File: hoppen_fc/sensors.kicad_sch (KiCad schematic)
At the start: 12 parts, among them U2 MMC5983MA, U3 BMI088, U4 MS5607-02BA

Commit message: finished adding lcsc numbers
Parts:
- added S1: ~, 0_misc:right_hand_rule, symbol 0_misc:right_hand_rule
- C53: renamed from C28; LCSC (none) -> C19666
- C54: renamed from C30; LCSC (none) -> C307331
- C55: renamed from C31; LCSC (none) -> C307331
- C56: renamed from C34; LCSC (none) -> C19666
- C57: renamed from C35; LCSC (none) -> C307331
- C58: renamed from C27; LCSC (none) -> C19666
- C59: renamed from C29; LCSC (none) -> C307331
- C60: renamed from C32; LCSC (none) -> C307331
- C61: renamed from C33; LCSC (none) -> C307331
- renumbered U4 to U7, U3 to U8, U2 to U9

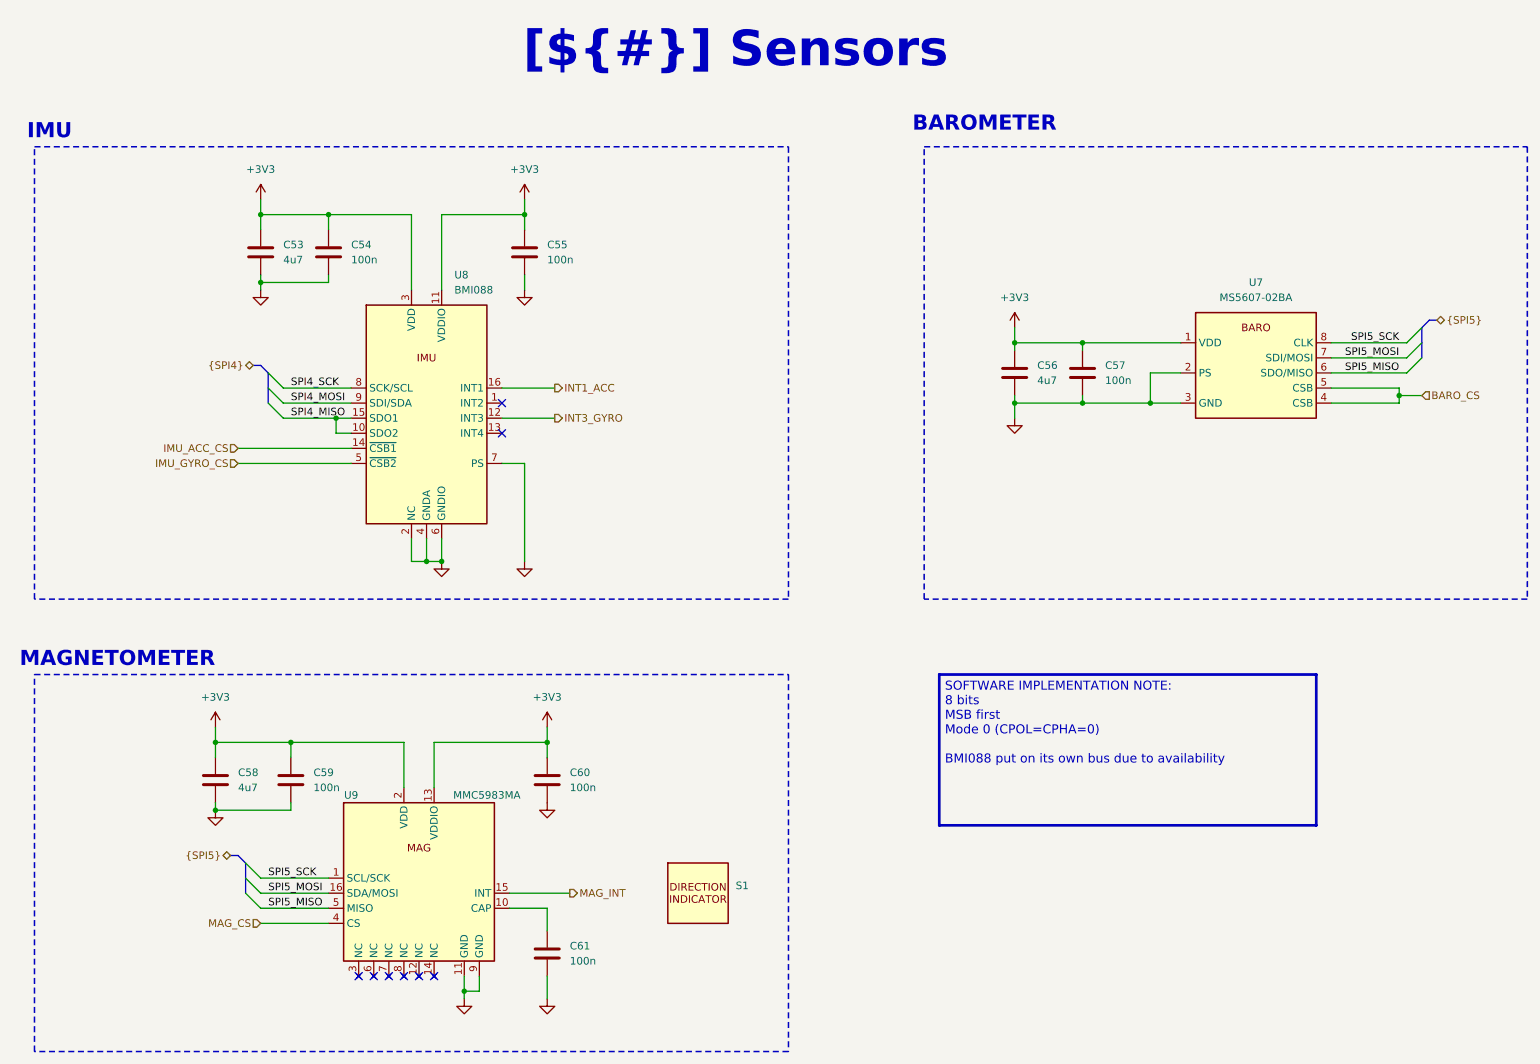
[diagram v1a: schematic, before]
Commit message: routing and adding rf module
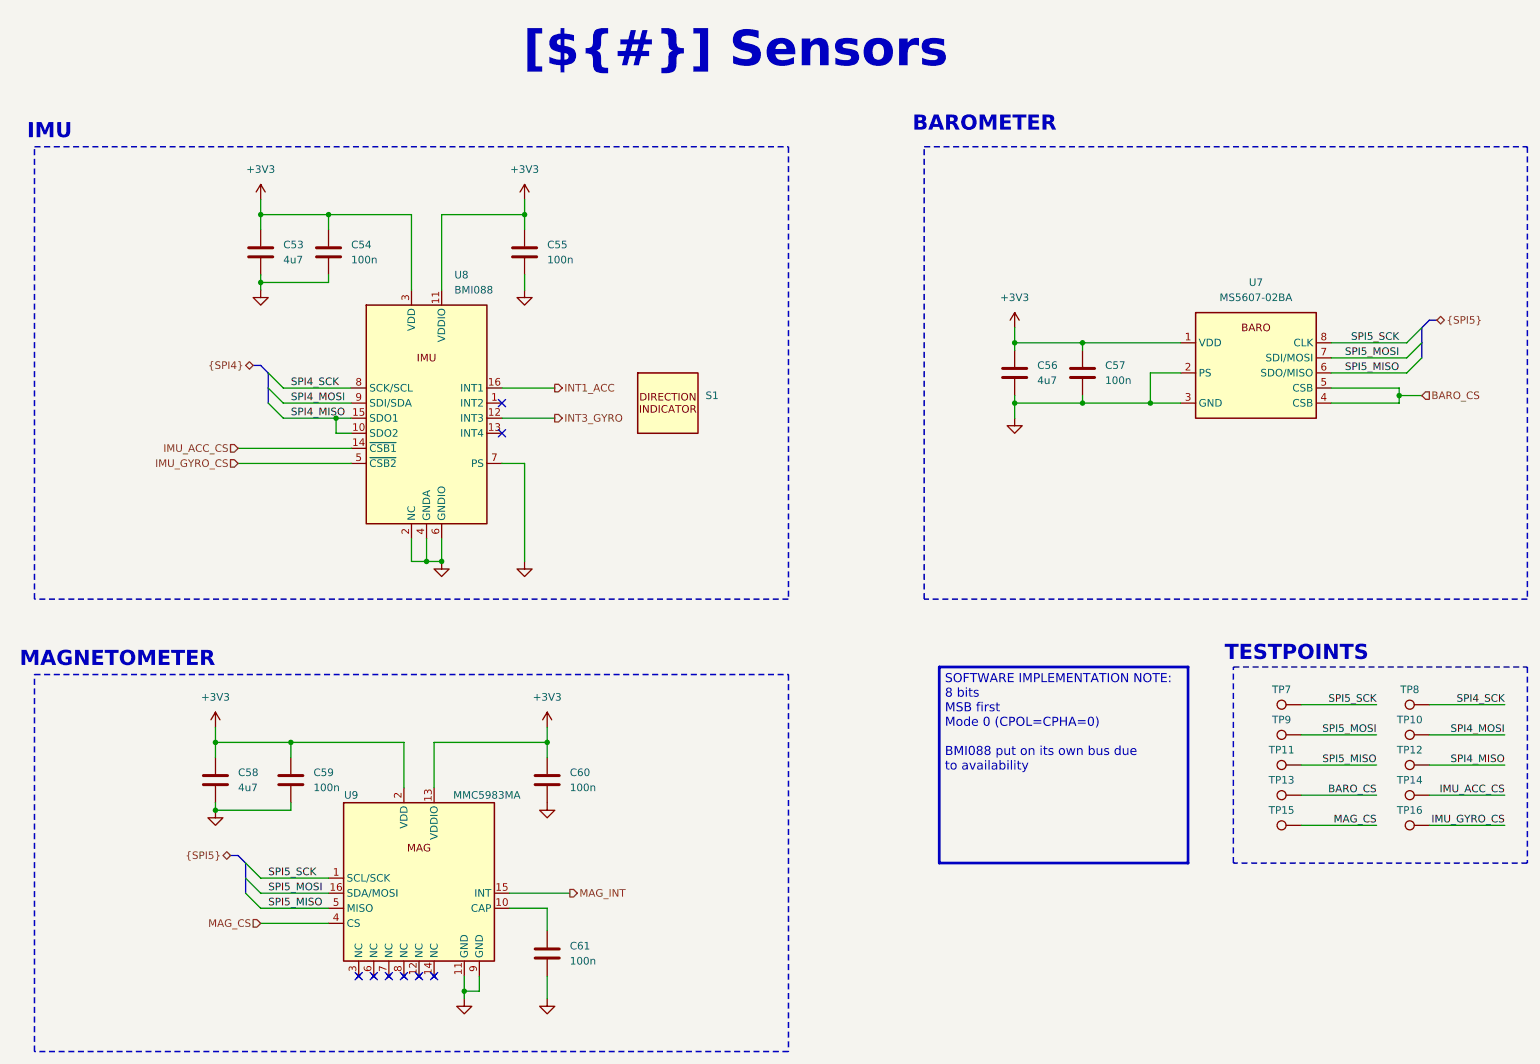
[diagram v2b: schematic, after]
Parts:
- added TP10, TP11, TP12, TP13, TP14, TP15, TP16, TP7, TP8, TP9: TestPoint, TestPoint:TestPoint_Pad_1.0x1.0mm, symbol Connector:TestPoint
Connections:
- net BARO_CS: now also TP13.1
- net IMU_ACC_CS: now also TP14.1
- net IMU_GYRO_CS: now also TP16.1
- net MAG_CS: now also TP15.1
- net SPI4_MISO: now also TP12.1
- net SPI4_MOSI: now also TP10.1
- net SPI4_SCK: now also TP8.1
- net SPI5_MISO: now also TP11.1
- net SPI5_MOSI: now also TP9.1
- net SPI5_SCK: now also TP7.1
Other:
- note added: "TESTPOINTS"
- moved on the sheet: S1

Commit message: bump
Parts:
- renumbered TP11 to TP10, TP12 to TP11, TP13 to TP12, TP14 to TP13, TP15 to TP14, TP16 to TP15, TP7 to TP6, TP8 to TP7, TP9 to TP8, TP10 to TP9
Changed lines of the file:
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@@
 		(dnp no)
 		(fields_autoplaced yes)
-		(property "Reference" "TP14"
+		(property "Reference" "TP13"
 			(at 257.048 144.78 90)
 			(effects
@@
 			(project "hoppen_fc"
 				(path "/abe950a1-9eef-4508-9fd4-31d3e723e029/c85454e5-a89e-41eb-a5ed-71b4fc4cf13a/328607b5-eaf8-4cbb-82fe-138ea1b53a88"
-					(reference "TP14")
+					(reference "TP13")
 					(unit 1)
 				)
@@
 		(dnp no)
 		(fields_autoplaced yes)
-		(property "Reference" "TP11"
+		(property "Reference" "TP10"
 			(at 235.458 139.7 90)
 			(effects
@@
 			(project "hoppen_fc"
 				(path "/abe950a1-9eef-4508-9fd4-31d3e723e029/c85454e5-a89e-41eb-a5ed-71b4fc4cf13a/328607b5-eaf8-4cbb-82fe-138ea1b53a88"
-					(reference "TP11")
+					(reference "TP10")
 					(unit 1)
 				)
@@
 		(dnp no)
 		(fields_autoplaced yes)
-		(property "Reference" "TP16"
+		(property "Reference" "TP15"
 			(at 257.048 149.86 90)
 			(effects
@@
 			(project "hoppen_fc"
 				(path "/abe950a1-9eef-4508-9fd4-31d3e723e029/c85454e5-a89e-41eb-a5ed-71b4fc4cf13a/328607b5-eaf8-4cbb-82fe-138ea1b53a88"
-					(reference "TP16")
+					(reference "TP15")
 					(unit 1)
 				)
@@
 		(dnp no)
 		(fields_autoplaced yes)
-		(property "Reference" "TP13"
+		(property "Reference" "TP12"
 			(at 235.458 144.78 90)
 			(effects
@@
 			(project "hoppen_fc"
 				(path "/abe950a1-9eef-4508-9fd4-31d3e723e029/c85454e5-a89e-41eb-a5ed-71b4fc4cf13a/328607b5-eaf8-4cbb-82fe-138ea1b53a88"
-					(reference "TP13")
+					(reference "TP12")
 					(unit 1)
 				)
@@
 		(dnp no)
 		(fields_autoplaced yes)
-		(property "Reference" "TP7"
+		(property "Reference" "TP6"
 			(at 235.458 129.54 90)
 			(effects
@@
 			(project "hoppen_fc"
 				(path "/abe950a1-9eef-4508-9fd4-31d3e723e029/c85454e5-a89e-41eb-a5ed-71b4fc4cf13a/328607b5-eaf8-4cbb-82fe-138ea1b53a88"
-					(reference "TP7")
+					(reference "TP6")
 					(unit 1)
 				)
@@
 		(dnp no)
 		(fields_autoplaced yes)
-		(property "Reference" "TP15"
+		(property "Reference" "TP14"
 			(at 235.458 149.86 90)
 			(effects
@@
 			(project "hoppen_fc"
 				(path "/abe950a1-9eef-4508-9fd4-31d3e723e029/c85454e5-a89e-41eb-a5ed-71b4fc4cf13a/328607b5-eaf8-4cbb-82fe-138ea1b53a88"
-					(reference "TP15")
+					(reference "TP14")
 					(unit 1)
 				)
@@
 		(dnp no)
 		(fields_autoplaced yes)
-		(property "Reference" "TP10"
+		(property "Reference" "TP9"
 			(at 257.048 134.62 90)
 			(effects
@@
 			(project "hoppen_fc"
 				(path "/abe950a1-9eef-4508-9fd4-31d3e723e029/c85454e5-a89e-41eb-a5ed-71b4fc4cf13a/328607b5-eaf8-4cbb-82fe-138ea1b53a88"
-					(reference "TP10")
+					(reference "TP9")
 					(unit 1)
 				)
@@
 		(dnp no)
 		(fields_autoplaced yes)
-		(property "Reference" "TP12"
+		(property "Reference" "TP11"
 			(at 257.048 139.7 90)
 			(effects
@@
 			(project "hoppen_fc"
 				(path "/abe950a1-9eef-4508-9fd4-31d3e723e029/c85454e5-a89e-41eb-a5ed-71b4fc4cf13a/328607b5-eaf8-4cbb-82fe-138ea1b53a88"
-					(reference "TP12")
+					(reference "TP11")
 					(unit 1)
 				)
@@
 		(dnp no)
 		(fields_autoplaced yes)
-		(property "Reference" "TP9"
+		(property "Reference" "TP8"
 			(at 235.458 134.62 90)
 			(effects
@@
 			(project "hoppen_fc"
 				(path "/abe950a1-9eef-4508-9fd4-31d3e723e029/c85454e5-a89e-41eb-a5ed-71b4fc4cf13a/328607b5-eaf8-4cbb-82fe-138ea1b53a88"
-					(reference "TP9")
+					(reference "TP8")
 					(unit 1)
 				)
@@
 		(dnp no)
 		(fields_autoplaced yes)
-		(property "Reference" "TP8"
+		(property "Reference" "TP7"
 			(at 257.048 129.54 90)
 			(effects
@@
 			(project "hoppen_fc"
 				(path "/abe950a1-9eef-4508-9fd4-31d3e723e029/c85454e5-a89e-41eb-a5ed-71b4fc4cf13a/328607b5-eaf8-4cbb-82fe-138ea1b53a88"
-					(reference "TP8")
-					(unit 1)
-				)
+					(reference "TP7")
+					(unit 1)
+				)

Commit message: bump
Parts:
- removed C53, C56: 4u7, 0_capacitor_smd:C_0603_1608Metric, symbol Device:C
- removed C54, C55, C57, C59, C61: 100n, 0_capacitor_smd:C_0402_1005Metric, symbol Device:C
- added C46, C47, C48: 100n, 0_capacitor_smd:C_0402_1005Metric, symbol Device:C
- added C51: 10u, 0_capacitor_smd:C_0805_2012Metric, symbol Device:C
- added TP17, TP18, TP19: TestPoint, TestPoint:TestPoint_Pad_1.0x1.0mm, symbol Connector:TestPoint
- C49: renamed from C58; value 4u7 -> 1u; footprint 0_capacitor_smd:C_0603_1608Metric -> 0_capacitor_smd:C_0402_1005Metric; LCSC C19666 -> C52923
- renumbered C60 to C50, TP9 to TP10, TP10 to TP11, TP11 to TP12, TP12 to TP13, TP13 to TP14, TP14 to TP15, TP15 to TP16, TP6 to TP7, TP7 to TP8, TP8 to TP9, U9 to U10, U7 to U8, U8 to U9
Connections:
- net +3V3: now also C46.1, C47.1, C48.1
- net GND: now also C46.2, C47.2, C48.2, C51.1
- net INT1_ACC: now also TP18.1
- net INT3_GYRO: now also TP19.1
- net MAG_INT: now also TP17.1
- net SPI4_MISO: now also U10.5 (MISO), U8.6 (SDO/MISO); no longer U9.10 (SDO2), U9.15 (SDO1)
- net SPI4_MOSI: now also U10.16 (SDA/MOSI), U8.7 (SDI/MOSI); no longer U9.9 (SDI/SDA)
- net SPI4_SCK: now also U10.1 (SCL/SCK), U8.8 (CLK); no longer U9.8 (SCK/SCL)
- net MAG_CAP: now reaches U10.10 (CAP)
- net MAG_CAP: now also C51.2
- removed net SPI5_MISO: TP11.1, U10.5 (MISO), U8.6 (SDO/MISO)
- removed net SPI5_MOSI: TP9.1, U10.16 (SDA/MOSI), U8.7 (SDI/MOSI)
- removed net SPI5_SCK: TP7.1, U10.1 (SCL/SCK), U8.8 (CLK)
- new net SPI1_MISO: TP11.1, U9.10 (SDO2), U9.15 (SDO1)
- new net SPI1_MOSI: TP9.1, U9.9 (SDI/SDA)
- new net SPI1_SCK: TP7.1, U9.8 (SCK/SCL)
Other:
- moved on the sheet: C49, TP10, TP11, TP12, TP13, TP14, TP15, TP16, TP7, TP8, TP9

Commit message: bump
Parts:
- added S2: ~, 0_misc:right_hand_rule_2, symbol 0_misc:right_hand_rule
- renumbered TP7 to TP23, TP8 to TP24, TP9 to TP25, TP10 to TP26, TP11 to TP27, TP12 to TP28, TP13 to TP29, TP14 to TP30, TP15 to TP31, TP16 to TP32, TP17 to TP33, TP18 to TP34, TP19 to TP35
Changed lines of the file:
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@@
+	)
+	(symbol
+		(lib_id "0_misc:right_hand_rule")
+		(at 134.62 165.1 0)
+		(unit 1)
+		(exclude_from_sim no)
+		(in_bom no)
+		(on_board yes)
+		(dnp no)
+		(fields_autoplaced yes)
+		(property "Reference" "S2"
+			(at 140.97 163.8299 0)
+			(effects
+				(font
+					(size 1.27 1.27)
+				)
+				(justify left)
+			)
+		)
+		(property "Value" "~"
+			(at 140.97 166.3699 0)
+			(effects
+				(font
+					(size 1.27 1.27)
+				)
+				(justify left)
+				(hide yes)
+			)
+		)
+		(property "Footprint" "0_misc:right_hand_rule_2"
+			(at 134.62 165.1 0)
+			(effects
+				(font
+					(size 1.27 1.27)
+				)
+				(hide yes)
+			)
+		)
+		(property "Datasheet" ""
+			(at 134.62 165.1 0)
+			(effects
+				(font
+					(size 1.27 1.27)
+				)
+				(hide yes)
+			)
+		)
+		(property "Description" ""
+			(at 134.62 165.1 0)
+			(effects
+				(font
+					(size 1.27 1.27)
+				)
+				(hide yes)
+			)
+		)
+		(instances
+			(project "hoppen_fc"
+				(path "/abe950a1-9eef-4508-9fd4-31d3e723e029/c85454e5-a89e-41eb-a5ed-71b4fc4cf13a/328607b5-eaf8-4cbb-82fe-138ea1b53a88"
+					(reference "S2")
+					(unit 1)
+				)
+			)
+		)
 	)
 	(symbol
@@
 		(dnp no)
 		(fields_autoplaced yes)
-		(property "Reference" "TP14"
+		(property "Reference" "TP30"
 			(at 257.048 142.24 90)
 			(effects
@@
 			(project "hoppen_fc"
 				(path "/abe950a1-9eef-4508-9fd4-31d3e723e029/c85454e5-a89e-41eb-a5ed-71b4fc4cf13a/328607b5-eaf8-4cbb-82fe-138ea1b53a88"
-					(reference "TP14")
+					(reference "TP30")
 					(unit 1)
 				)
@@
 		(dnp no)
 		(fields_autoplaced yes)
-		(property "Reference" "TP17"
+		(property "Reference" "TP33"
 			(at 235.458 152.4 90)
 			(effects
@@
 			(project "hoppen_fc"
 				(path "/abe950a1-9eef-4508-9fd4-31d3e723e029/c85454e5-a89e-41eb-a5ed-71b4fc4cf13a/328607b5-eaf8-4cbb-82fe-138ea1b53a88"
-					(reference "TP17")
+					(reference "TP33")
 					(unit 1)
 				)
@@
 		(dnp no)
 		(fields_autoplaced yes)
-		(property "Reference" "TP18"
+		(property "Reference" "TP34"
 			(at 257.048 152.4 90)
 			(effects
@@
 			(project "hoppen_fc"
 				(path "/abe950a1-9eef-4508-9fd4-31d3e723e029/c85454e5-a89e-41eb-a5ed-71b4fc4cf13a/328607b5-eaf8-4cbb-82fe-138ea1b53a88"
-					(reference "TP18")
+					(reference "TP34")
 					(unit 1)
 				)
@@
 		(dnp no)
 		(fields_autoplaced yes)
-		(property "Reference" "TP11"
+		(property "Reference" "TP27"
 			(at 235.458 137.16 90)
 			(effects
@@
 			(project "hoppen_fc"
 				(path "/abe950a1-9eef-4508-9fd4-31d3e723e029/c85454e5-a89e-41eb-a5ed-71b4fc4cf13a/328607b5-eaf8-4cbb-82fe-138ea1b53a88"
-					(reference "TP11")
+					(reference "TP27")
 					(unit 1)
 				)
@@
 		(dnp no)
 		(fields_autoplaced yes)
-		(property "Reference" "TP16"
+		(property "Reference" "TP32"
 			(at 257.048 147.32 90)
 			(effects
@@
 			(project "hoppen_fc"
 				(path "/abe950a1-9eef-4508-9fd4-31d3e723e029/c85454e5-a89e-41eb-a5ed-71b4fc4cf13a/328607b5-eaf8-4cbb-82fe-138ea1b53a88"
-					(reference "TP16")
+					(reference "TP32")
 					(unit 1)
 				)
@@
 		(dnp no)
 		(fields_autoplaced yes)
-		(property "Reference" "TP13"
+		(property "Reference" "TP29"
 			(at 235.458 142.24 90)
 			(effects
@@
 			(project "hoppen_fc"
 				(path "/abe950a1-9eef-4508-9fd4-31d3e723e029/c85454e5-a89e-41eb-a5ed-71b4fc4cf13a/328607b5-eaf8-4cbb-82fe-138ea1b53a88"
-					(reference "TP13")
+					(reference "TP29")
 					(unit 1)
 				)
@@
 		(dnp no)
 		(fields_autoplaced yes)
-		(property "Reference" "TP7"
+		(property "Reference" "TP23"
 			(at 235.458 127 90)
 			(effects
@@
 			(project "hoppen_fc"
 				(path "/abe950a1-9eef-4508-9fd4-31d3e723e029/c85454e5-a89e-41eb-a5ed-71b4fc4cf13a/328607b5-eaf8-4cbb-82fe-138ea1b53a88"
-					(reference "TP7")
+					(reference "TP23")
 					(unit 1)
 				)
@@
 		(dnp no)
 		(fields_autoplaced yes)
-		(property "Reference" "TP15"
+		(property "Reference" "TP31"
 			(at 235.458 147.32 90)
 			(effects
@@
 			(project "hoppen_fc"
 				(path "/abe950a1-9eef-4508-9fd4-31d3e723e029/c85454e5-a89e-41eb-a5ed-71b4fc4cf13a/328607b5-eaf8-4cbb-82fe-138ea1b53a88"
-					(reference "TP15")
+					(reference "TP31")
 					(unit 1)
 				)
@@
 		(dnp no)
 		(fields_autoplaced yes)
-		(property "Reference" "TP10"
+		(property "Reference" "TP26"
 			(at 257.048 132.08 90)
 			(effects
@@
 			(project "hoppen_fc"
 				(path "/abe950a1-9eef-4508-9fd4-31d3e723e029/c85454e5-a89e-41eb-a5ed-71b4fc4cf13a/328607b5-eaf8-4cbb-82fe-138ea1b53a88"
-					(reference "TP10")
+					(reference "TP26")
 					(unit 1)
 				)
@@
 		(dnp no)
 		(fields_autoplaced yes)
-		(property "Reference" "TP12"
+		(property "Reference" "TP28"
 			(at 257.048 137.16 90)
 			(effects
@@
 			(project "hoppen_fc"
 				(path "/abe950a1-9eef-4508-9fd4-31d3e723e029/c85454e5-a89e-41eb-a5ed-71b4fc4cf13a/328607b5-eaf8-4cbb-82fe-138ea1b53a88"
-					(reference "TP12")
+					(reference "TP28")
 					(unit 1)
 				)
@@
 		(on_board yes)
 		(dnp no)
-		(property "Reference" "TP19"
+		(property "Reference" "TP35"
 			(at 235.458 157.48 90)
 			(effects
@@
 			(project "hoppen_fc"
 				(path "/abe950a1-9eef-4508-9fd4-31d3e723e029/c85454e5-a89e-41eb-a5ed-71b4fc4cf13a/328607b5-eaf8-4cbb-82fe-138ea1b53a88"
-					(reference "TP19")
+					(reference "TP35")
 					(unit 1)
 				)
@@
 		(dnp no)
 		(fields_autoplaced yes)
-		(property "Reference" "TP9"
+		(property "Reference" "TP25"
 			(at 235.458 132.08 90)
 			(effects
@@
 			(project "hoppen_fc"
 				(path "/abe950a1-9eef-4508-9fd4-31d3e723e029/c85454e5-a89e-41eb-a5ed-71b4fc4cf13a/328607b5-eaf8-4cbb-82fe-138ea1b53a88"
-					(reference "TP9")
+					(reference "TP25")
 					(unit 1)
 				)
@@
 		(dnp no)
 		(fields_autoplaced yes)
-		(property "Reference" "TP8"
+		(property "Reference" "TP24"
 			(at 257.048 127 90)
 			(effects
@@
 			(project "hoppen_fc"
 				(path "/abe950a1-9eef-4508-9fd4-31d3e723e029/c85454e5-a89e-41eb-a5ed-71b4fc4cf13a/328607b5-eaf8-4cbb-82fe-138ea1b53a88"
-					(reference "TP8")
-					(unit 1)
-				)
+					(reference "TP24")
+					(unit 1)
+				)
